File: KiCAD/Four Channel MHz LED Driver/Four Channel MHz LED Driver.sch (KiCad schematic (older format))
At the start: 92 parts, among them J1 Barrel_Jack_Switch, J10 Conn_01x24_Female, J2 Conn_01x02_Female, J3 8P8C_Shielded_x4, J4 Conn_01x03_Male, J5 Conn_01x03_Female, J6 Conn_01x08_Female, J7 Conn_01x03_Female, J8 Conn_01x05_Female, J9 Conn_01x24_Female, M1 Fan_4pin, Q1 SUM70060E, SW1 Pushbutton_with_LED, SW2 Pushbutton_with_LED, SW3 Pushbutton_with_LED, SW4 Pushbutton_with_LED, SW5 SW_SPDT, U1 12V boost, U10 ASSR-1218, U11 ASSR-1218, U12 Teensy3.6, U2 SN74LV4T125PWR, U3 DPBW06F-05, U4 TMUX1204DGSR, U5 BDJ0GA5WEFJ-E2, U6 ADP7182AUJZ-1.8-R7, U7 LT6200CS8-10, U8 ASSR-1218, U9 ASSR-1218

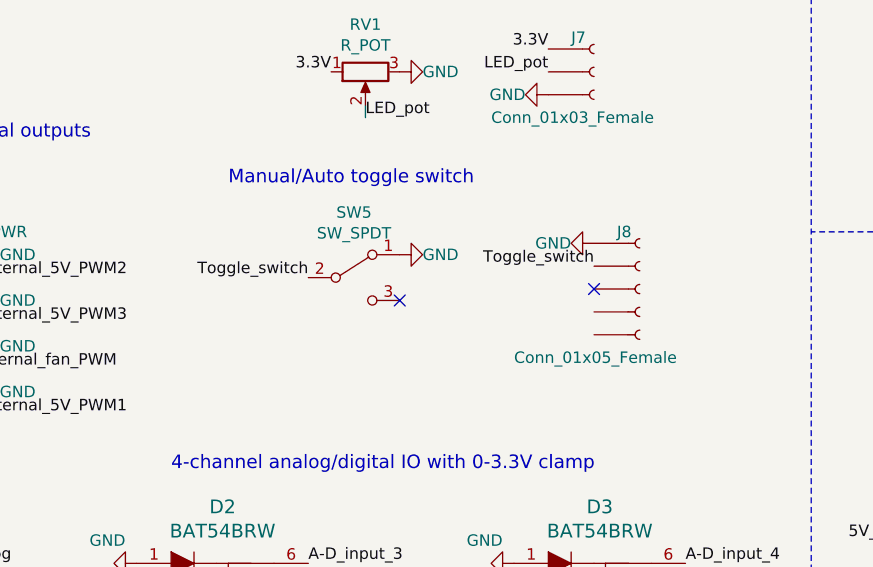
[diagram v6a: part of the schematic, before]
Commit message: Fix 4.7kx8 footprint
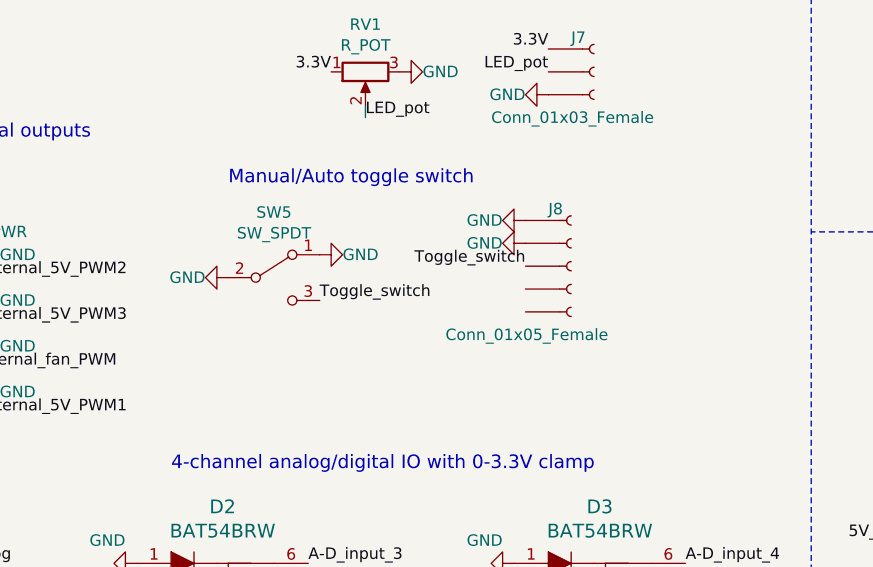
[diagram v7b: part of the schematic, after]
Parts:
- RN3: footprint Custom Footprints:2506_8x_R-pack -> Custom Footprints:2506_modified_concave_8x_R-pack
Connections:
- net GND: now also SW5.2 (B)
- net Toggle_switch: now also SW5.3 (C); no longer SW5.2 (B)
- no-connect marks 51 -> 49
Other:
- moved on the sheet: J8, SW5
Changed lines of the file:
@@
 F 1 "BAT54BRW" H 5775 11091 60  0000 C CNN
 F 2 "Package_TO_SOT_SMD:SOT-363_SC-70-6" H 5800 11050 60  0001 L CNN
-F 3 "https://www.diodes.com/assets/Datasheets/ds11005.pdf" H 5800 11150 60  0001 L CNN
+F 3 "https://www.diodes.com/assets/Datasheets/ds30152.pdf" H 5800 11150 60  0001 L CNN
 F 4 "Diodes Incorporated" H 5600 10850 50  0001 C CNN "Manufacturer"
 F 5 "BAT54BRW-7-F" H 5600 10850 50  0001 C CNN "Part #"
@@
 L Switch:SW_SPDT SW5
 U 1 1 5F6733E8
-P 4700 9500
-F 0 "SW5" H 4700 9785 50  0000 C CNN
-F 1 "SW_SPDT" H 4700 9694 50  0000 C CNN
-F 2 "Custom Footprints:1x5_header_SSM-105-L-SV-BE-LC" H 4700 9500 50  0001 C CNN
-F 3 "https://sten-eswitch-13110800-production.s3.amazonaws.com/system/asset/product_line/data_sheet/131/200.pdf" H 4700 9500 50  0001 C CNN
-F 4 "E-Switch" H 4700 9500 50  0001 C CNN "Manufacturer"
-F 5 "200MSP1T1B1M7QE" H 4700 9500 50  0001 C CNN "Part #"
-	1    4700 9500
+P 4350 9500
+F 0 "SW5" H 4350 9785 50  0000 C CNN
+F 1 "SW_SPDT" H 4350 9694 50  0000 C CNN
+F 2 "Custom Footprints:1x5_header_SSM-105-L-SV-BE-LC" H 4350 9500 50  0001 C CNN
+F 3 "https://sten-eswitch-13110800-production.s3.amazonaws.com/system/asset/product_line/data_sheet/131/200.pdf" H 4350 9500 50  0001 C CNN
+F 4 "E-Switch" H 4350 9500 50  0001 C CNN "Manufacturer"
+F 5 "200MSP1T1B1M7QE" H 4350 9500 50  0001 C CNN "Part #"
+	1    4350 9500
 	1    0    0    -1
 $EndComp
-Text Label 5750 9450 2    50   ~ 0
+Text Label 5450 9450 2    50   ~ 0
 Toggle_switch
 $Comp
 L power:GND #PWR056
 U 1 1 5F678CF5
-P 4900 9400
-F 0 "#PWR056" H 4900 9150 50  0001 C CNN
-F 1 "GND" V 4900 9300 50  0000 R CNN
-F 2 "" H 4900 9400 50  0001 C CNN
-F 3 "" H 4900 9400 50  0001 C CNN
-	1    4900 9400
+P 4550 9400
+F 0 "#PWR056" H 4550 9150 50  0001 C CNN
+F 1 "GND" V 4550 9300 50  0000 R CNN
+F 2 "" H 4550 9400 50  0001 C CNN
+F 3 "" H 4550 9400 50  0001 C CNN
+	1    4550 9400
 	0    -1   -1   0
 $EndComp
@@
 L power:GND #PWR065
 U 1 1 5F68BFE7
-P 5750 9350
-F 0 "#PWR065" H 5750 9100 50  0001 C CNN
-F 1 "GND" V 5750 9250 50  0000 R CNN
-F 2 "" H 5750 9350 50  0001 C CNN
-F 3 "" H 5750 9350 50  0001 C CNN
-	1    5750 9350
+P 5450 9250
+F 0 "#PWR065" H 5450 9000 50  0001 C CNN
+F 1 "GND" V 5450 9150 50  0000 R CNN
+F 2 "" H 5450 9250 50  0001 C CNN
+F 3 "" H 5450 9250 50  0001 C CNN
+	1    5450 9250
 	0    1    1    0
 $EndComp
@@
 L Custom_parts:Conn_01x05_Female J8
 U 1 1 5F6C332D
-P 5950 9550
-F 0 "J8" H 5850 9800 50  0000 L CNN
-F 1 "Conn_01x05_Female" H 5400 9250 50  0000 L CNN
-F 2 "Custom Footprints:Ref_only" H 5950 9550 50  0001 C CNN
-F 3 "http://suddendocs.samtec.com/prints/ssm-1xx-xxx-xx-xx-xx-x-xx-footprint.pdf" H 5950 9550 50  0001 C CNN
-F 4 "Samtec Inc." H 5950 9550 50  0001 C CNN "Manufacturer"
-F 5 "SSM-105-L-SV-BE-LC-TR" H 5950 9550 50  0001 C CNN "Part #"
-	1    5950 9550
+P 5650 9450
+F 0 "J8" H 5550 9700 50  0000 L CNN
+F 1 "Conn_01x05_Female" H 5100 9150 50  0000 L CNN
+F 2 "Custom Footprints:Ref_only" H 5650 9450 50  0001 C CNN
+F 3 "http://suddendocs.samtec.com/prints/ssm-1xx-xxx-xx-xx-xx-x-xx-footprint.pdf" H 5650 9450 50  0001 C CNN
+F 4 "Samtec Inc." H 5650 9450 50  0001 C CNN "Manufacturer"
+F 5 "SSM-105-L-SV-BE-LC-TR" H 5650 9450 50  0001 C CNN "Part #"
+	1    5650 9450
 	1    0    0    -1
 $EndComp
@@
 Text Label 6250 5850 0    50   ~ 0
 LED4
-NoConn ~ 5750 9550
-NoConn ~ 4900 9600
 $Comp
 L Device:R_Pack08_Split RN1
@@
 F 1 "BAT54BRW" H 4125 11091 60  0000 C CNN
 F 2 "Package_TO_SOT_SMD:SOT-363_SC-70-6" H 4150 11050 60  0001 L CNN
-F 3 "https://www.diodes.com/assets/Datasheets/ds11005.pdf" H 4150 11150 60  0001 L CNN
+F 3 "https://www.diodes.com/assets/Datasheets/ds30152.pdf" H 4150 11150 60  0001 L CNN
 F 4 "Diodes Incorporated" H 3950 10850 50  0001 C CNN "Manufacturer"
 F 5 "BAT54BRW-7-F" H 3950 10850 50  0001 C CNN "Part #"
@@
 F 1 "BAT54BRW" H 2275 11091 60  0000 C CNN
 F 2 "Package_TO_SOT_SMD:SOT-363_SC-70-6" H 2300 11050 60  0001 L CNN
-F 3 "https://www.diodes.com/assets/Datasheets/ds11005.pdf" H 2300 11150 60  0001 L CNN
+F 3 "https://www.diodes.com/assets/Datasheets/ds30152.pdf" H 2300 11150 60  0001 L CNN
 F 4 "Diodes Incorporated" H 2100 10850 50  0001 C CNN "Manufacturer"
 F 5 "BAT54BRW-7-F" H 2100 10850 50  0001 C CNN "Part #"
@@
 F 0 "RN3" V 4700 7650 50  0000 C CNN
 F 1 "4.7k" V 4600 7650 50  0000 C CNN
-F 2 "Custom Footprints:2506_8x_R-pack" V 5075 7650 50  0001 C CNN
+F 2 "Custom Footprints:2506_modified_concave_8x_R-pack" V 5075 7650 50  0001 C CNN
 F 3 "https://www.ctscorp.com/wp-content/uploads/74x.pdf" H 4600 7650 50  0001 C CNN
 F 4 "CTS Resistor Products" V 4600 7650 50  0001 C CNN "Manufacturer"
@@
 F 0 "RN3" V 4500 7500 50  0000 C CNN
 F 1 "4.7k" V 4600 7500 50  0000 C CNN
-F 2 "Custom Footprints:2506_8x_R-pack" V 5075 7500 50  0001 C CNN
+F 2 "Custom Footprints:2506_modified_concave_8x_R-pack" V 5075 7500 50  0001 C CNN
 F 3 "https://www.ctscorp.com/wp-content/uploads/74x.pdf" H 4600 7500 50  0001 C CNN
 F 4 "CTS Resistor Products" V 4600 7500 50  0001 C CNN "Manufacturer"
@@
 F 0 "RN3" V 1900 7950 50  0000 C CNN
 F 1 "4.7k" V 2000 7950 50  0000 C CNN
-F 2 "Custom Footprints:2506_8x_R-pack" V 2475 7950 50  0001 C CNN
+F 2 "Custom Footprints:2506_modified_concave_8x_R-pack" V 2475 7950 50  0001 C CNN
 F 3 "https://www.ctscorp.com/wp-content/uploads/74x.pdf" H 2000 7950 50  0001 C CNN
 F 4 "CTS Resistor Products" V 2000 7950 50  0001 C CNN "Manufacturer"
@@
 F 0 "RN3" V 1900 8150 50  0000 C CNN
 F 1 "4.7k" V 2000 8150 50  0000 C CNN
-F 2 "Custom Footprints:2506_8x_R-pack" V 2475 8150 50  0001 C CNN
+F 2 "Custom Footprints:2506_modified_concave_8x_R-pack" V 2475 8150 50  0001 C CNN
 F 3 "https://www.ctscorp.com/wp-content/uploads/74x.pdf" H 2000 8150 50  0001 C CNN
 F 4 "CTS Resistor Products" V 2000 8150 50  0001 C CNN "Manufacturer"
@@
 F 0 "RN3" V 4700 7850 50  0000 C CNN
 F 1 "4.7k" V 4600 7850 50  0000 C CNN
-F 2 "Custom Footprints:2506_8x_R-pack" V 5075 7850 50  0001 C CNN
+F 2 "Custom Footprints:2506_modified_concave_8x_R-pack" V 5075 7850 50  0001 C CNN
 F 3 "https://www.ctscorp.com/wp-content/uploads/74x.pdf" H 4600 7850 50  0001 C CNN
 F 4 "CTS Resistor Products" V 4600 7850 50  0001 C CNN "Manufacturer"
@@
 F 0 "RN3" V 1900 8350 50  0000 C CNN
 F 1 "4.7k" V 2000 8350 50  0000 C CNN
-F 2 "Custom Footprints:2506_8x_R-pack" V 2475 8350 50  0001 C CNN
+F 2 "Custom Footprints:2506_modified_concave_8x_R-pack" V 2475 8350 50  0001 C CNN
 F 3 "https://www.ctscorp.com/wp-content/uploads/74x.pdf" H 2000 8350 50  0001 C CNN
 F 4 "CTS Resistor Products" V 2000 8350 50  0001 C CNN "Manufacturer"
@@
 	0    1    -1   0
 $EndComp
-$Comp
-L Device:R_Pack08_Split RN3
-U 4 1 5F6416DB
-P 2000 7750
-F 0 "RN3" V 1900 7750 50  0000 C CNN
-F 1 "4.7k" V 2000 7750 50  0000 C CNN
-F 2 "Custom Footprints:2506_8x_R-pack" V 2475 7750 50  0001 C CNN
-F 3 "https://www.ctscorp.com/wp-content/uploads/74x.pdf" H 2000 7750 50  0001 C CNN
-F 4 "CTS Resistor Products" V 2000 7750 50  0001 C CNN "Manufacturer"
-F 5 "742C163472JP" V 2000 7750 50  0001 C CNN "Part #"
-	4    2000 7750
-	0    1    -1   0
-$EndComp
 Connection ~ 4450 7850
 Connection ~ 4750 7850
@@
 Wire Wire Line
 	1600 6450 1850 6450
-Text Label 4500 9500 2    50   ~ 0
+Text Label 4550 9600 0    50   ~ 0
 Toggle_switch
 Text Label 2450 7050 0    50   ~ 0
@@
 F 0 "RN3" V 2850 9200 50  0000 C CNN
 F 1 "4.7k" V 2750 9200 50  0000 C CNN
-F 2 "Custom Footprints:2506_8x_R-pack" V 3225 9200 50  0001 C CNN
+F 2 "Custom Footprints:2506_modified_concave_8x_R-pack" V 3225 9200 50  0001 C CNN
 F 3 "https://www.ctscorp.com/wp-content/uploads/74x.pdf" H 2750 9200 50  0001 C CNN
 F 4 "CTS Resistor Products" V 2750 9200 50  0001 C CNN "Manufacturer"
@@
 	6050 2500 6100 2500
 Connection ~ 6050 2400
+$Comp
+L Device:R_Pack08_Split RN3
+U 4 1 5F6416DB
+P 2000 7750
+F 0 "RN3" V 1900 7750 50  0000 C CNN
+F 1 "4.7k" V 2000 7750 50  0000 C CNN
+F 2 "Custom Footprints:2506_modified_concave_8x_R-pack" V 2475 7750 50  0001 C CNN
+F 3 "https://www.ctscorp.com/wp-content/uploads/74x.pdf" H 2000 7750 50  0001 C CNN
+F 4 "CTS Resistor Products" V 2000 7750 50  0001 C CNN "Manufacturer"
+F 5 "742C163472JP" V 2000 7750 50  0001 C CNN "Part #"
+	4    2000 7750
+	0    1    -1   0
+$EndComp
+$Comp
+L power:GND #PWR?
+U 1 1 5F7CC92E
+P 4150 9500
+F 0 "#PWR?" H 4150 9250 50  0001 C CNN
+F 1 "GND" V 4150 9400 50  0000 R CNN
+F 2 "" H 4150 9500 50  0001 C CNN
+F 3 "" H 4150 9500 50  0001 C CNN
+	1    4150 9500
+	0    1    1    0
+$EndComp
+$Comp
+L power:GND #PWR?
+U 1 1 5F7CD122
+P 5450 9350
+F 0 "#PWR?" H 5450 9100 50  0001 C CNN
+F 1 "GND" V 5450 9250 50  0000 R CNN
+F 2 "" H 5450 9350 50  0001 C CNN
+F 3 "" H 5450 9350 50  0001 C CNN
+	1    5450 9350
+	0    1    1    0
+$EndComp
 $EndSCHEMATC

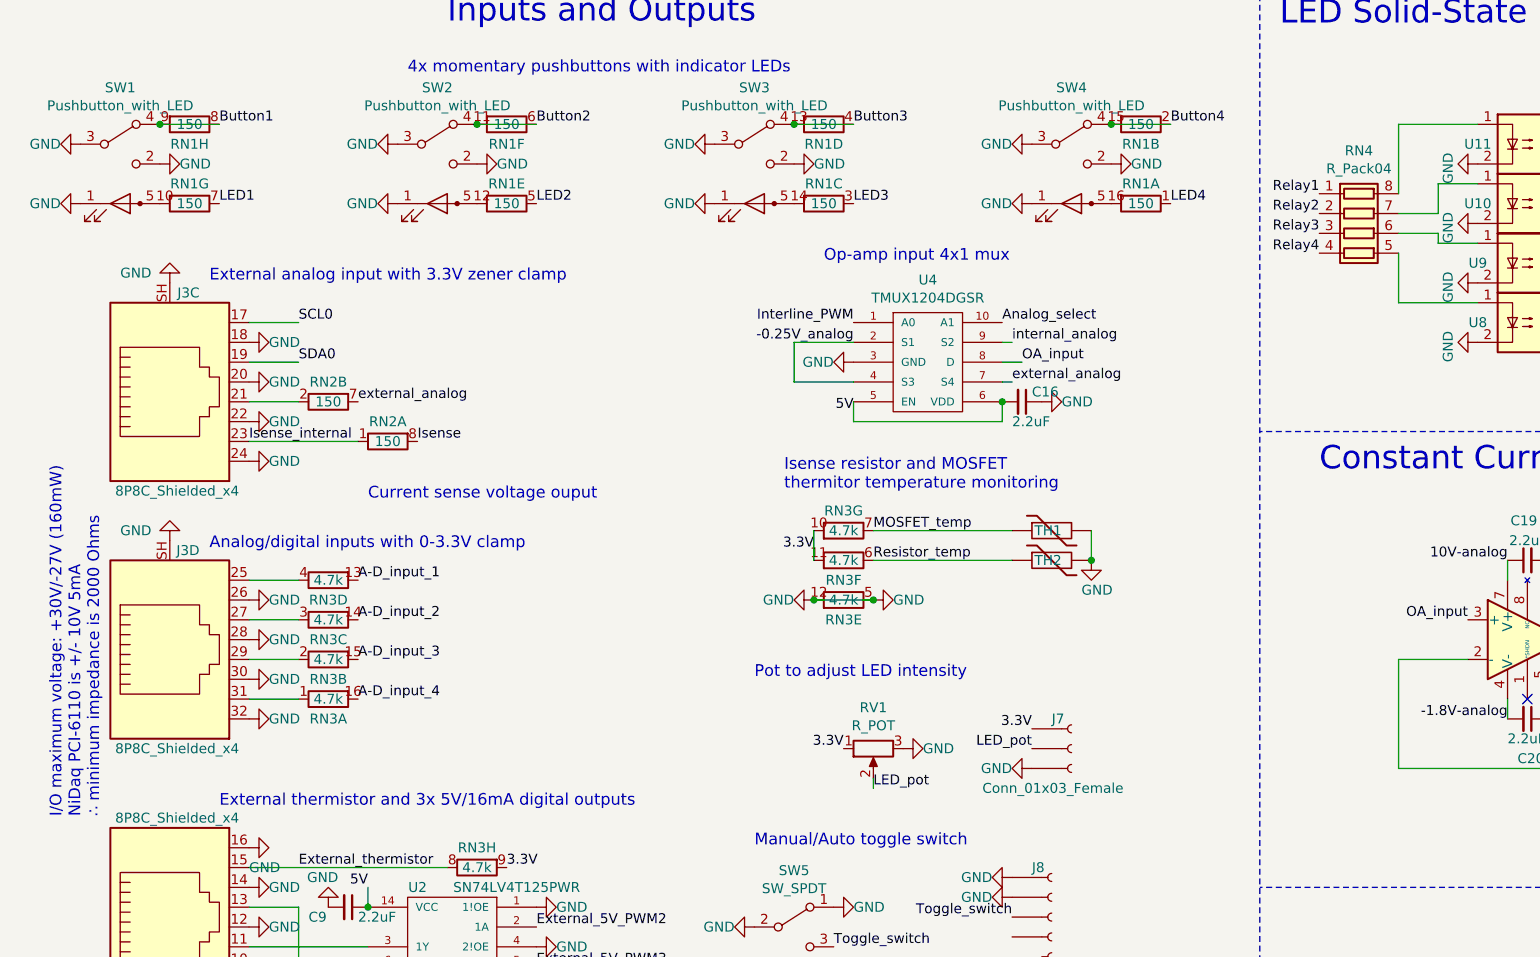
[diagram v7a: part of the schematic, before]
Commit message: Switch to 200 omh for relay to keep max current below 9 mA
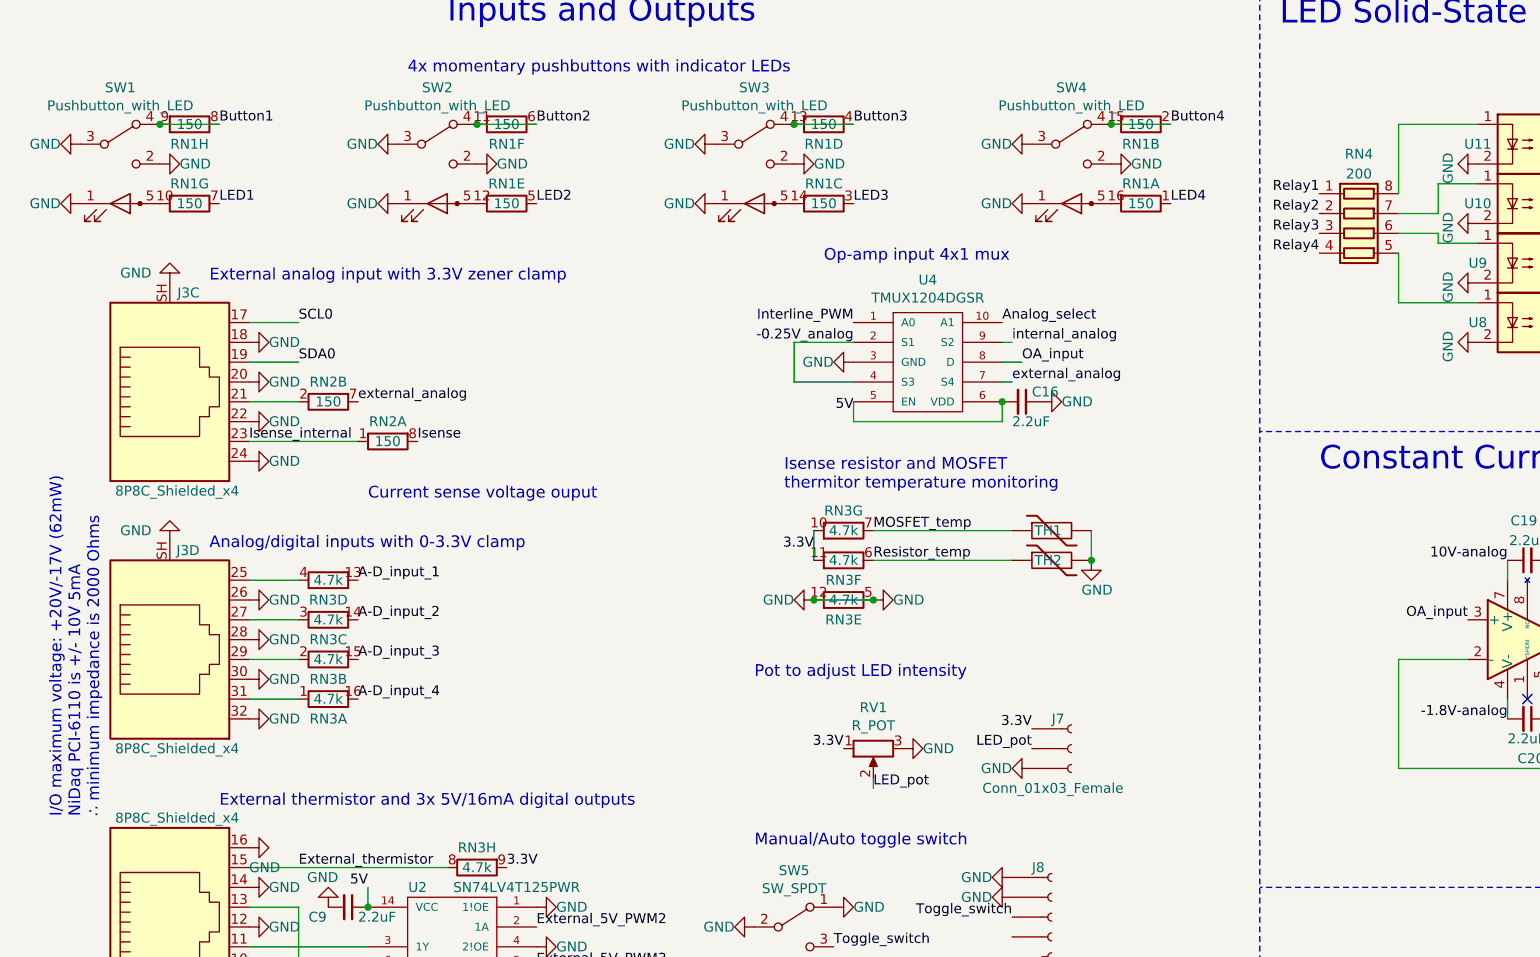
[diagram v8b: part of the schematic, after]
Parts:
- RN4: value R_Pack04 -> 200; Manufacturer Panasonic Electronic Components -> Yageo; Part # EXB-38V151JV -> YC164-JR-07200RL
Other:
- note added: "I/O maximum voltage: +20V/-17V (62mW)\nNiDaq PCI-6110 is +/- 10V 5mA\n∴ minimum impedance is 2000 Ohms"
- note removed: "I/O maximum voltage: +30V/-27V (160mW)\nNiDaq PCI-6110 is +/- 10V 5mA\n∴ minimum impedance is 2000 Ohms"
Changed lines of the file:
@@
 U 1 1 5F577F14
 P 7200 6000
-F 0 "RN4" V 6783 6000 50  0000 C CNN
-F 1 "R_Pack04" V 6874 6000 50  0000 C CNN
+F 0 "RN4" V 6800 6000 50  0000 C CNN
+F 1 "200" V 6900 6000 50  0000 C CNN
 F 2 "Resistor_SMD:R_Array_Convex_4x1206" V 7475 6000 50  0001 C CNN
 F 3 "https://industrial.panasonic.com/cdbs/www-data/pdf/AOC0000/AOC0000C14.pdf" H 7200 6000 50  0001 C CNN
-F 4 "Panasonic Electronic Components" V 7200 6000 50  0001 C CNN "Manufacturer"
-F 5 "EXB-38V151JV" V 7200 6000 50  0001 C CNN "Part #"
+F 4 "Yageo" V 7200 6000 50  0001 C CNN "Manufacturer"
+F 5 "YC164-JR-07200RL" V 7200 6000 50  0001 C CNN "Part #"
 	1    7200 6000
 	0    1    1    0
@@
 F 1 "Thermistor" H 5755 7605 50  0001 L CNN
 F 2 "Resistor_SMD:R_0603_1608Metric" H 5650 7650 50  0001 C CNN
-F 3 "https://ds.murata.co.jp/simsurfing/ntcthermistor.html?lcid=en-us" H 5650 7650 50  0001 C CNN
+F 3 "https://www.murata.com/products/productdata/8796839149598/NTHCG158.txt?1437969900000" H 5650 7650 50  0001 C CNN
 F 4 "Murata Electronics" H 5650 7650 50  0001 C CNN "Manufacturer"
 F 5 "NCP18XM472J03RB" H 5650 7650 50  0001 C CNN "Part #"
@@
 F 1 "Thermistor" H 5755 7455 50  0001 L CNN
 F 2 "Resistor_SMD:R_0603_1608Metric" H 5650 7500 50  0001 C CNN
-F 3 "https://ds.murata.co.jp/simsurfing/ntcthermistor.html?lcid=en-us" H 5650 7500 50  0001 C CNN
+F 3 "https://www.murata.com/products/productdata/8796839149598/NTHCG158.txt?1437969900000" H 5650 7500 50  0001 C CNN
 F 4 "Murata Electronics" H 5650 7500 50  0001 C CNN "Manufacturer"
 F 5 "NCP18XM472J03RB" H 5650 7500 50  0001 C CNN "Part #"
@@
 $EndComp
 Text Notes 850  8950 1    59   ~ 0
-I/O maximum voltage: +30V/-27V (160mW)\nNiDaq PCI-6110 is +/- 10V 5mA\n∴ minimum impedance is 2000 Ohms
+I/O maximum voltage: +20V/-17V (62mW)\nNiDaq PCI-6110 is +/- 10V 5mA\n∴ minimum impedance is 2000 Ohms
 Text Notes 4500 6150 0    59   ~ 0
 Op-amp input 4x1 mux
@@
 $EndComp
 $Comp
-L power:GND #PWR?
+L power:GND #PWR0101
 U 1 1 5F7CC92E
 P 4150 9500
-F 0 "#PWR?" H 4150 9250 50  0001 C CNN
+F 0 "#PWR0101" H 4150 9250 50  0001 C CNN
 F 1 "GND" V 4150 9400 50  0000 R CNN
 F 2 "" H 4150 9500 50  0001 C CNN
@@
 $EndComp
 $Comp
-L power:GND #PWR?
+L power:GND #PWR0102
 U 1 1 5F7CD122
 P 5450 9350
-F 0 "#PWR?" H 5450 9100 50  0001 C CNN
+F 0 "#PWR0102" H 5450 9100 50  0001 C CNN
 F 1 "GND" V 5450 9250 50  0000 R CNN
 F 2 "" H 5450 9350 50  0001 C CNN
